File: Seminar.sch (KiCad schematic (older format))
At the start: 0 parts

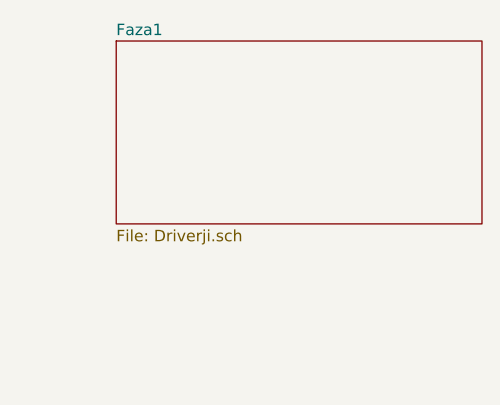
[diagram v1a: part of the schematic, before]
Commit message: Dokončal V-meter sheet in dodal A-meter sheet
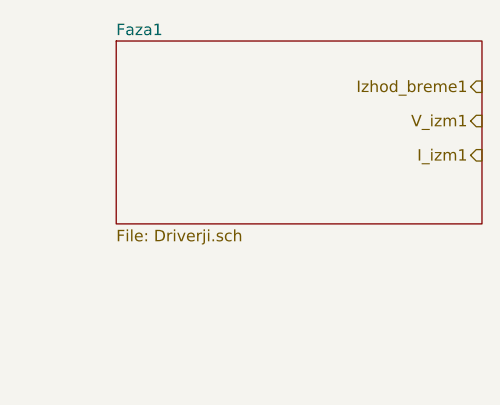
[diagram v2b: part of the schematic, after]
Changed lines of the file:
@@
 $Descr A4 11693 8268
 encoding utf-8
-Sheet 1 4
+Sheet 1 5
 Title ""
 Date ""
@@
 F1 "Driverji.sch" 50
 $EndSheet
+Text HLabel 10500 1450 0    50   Output ~ 0
+Izhod_breme1
+Text HLabel 10500 1600 0    50   Output ~ 0
+V_izm1
+Text HLabel 10500 1750 0    50   Output ~ 0
+I_izm1
 $EndSCHEMATC

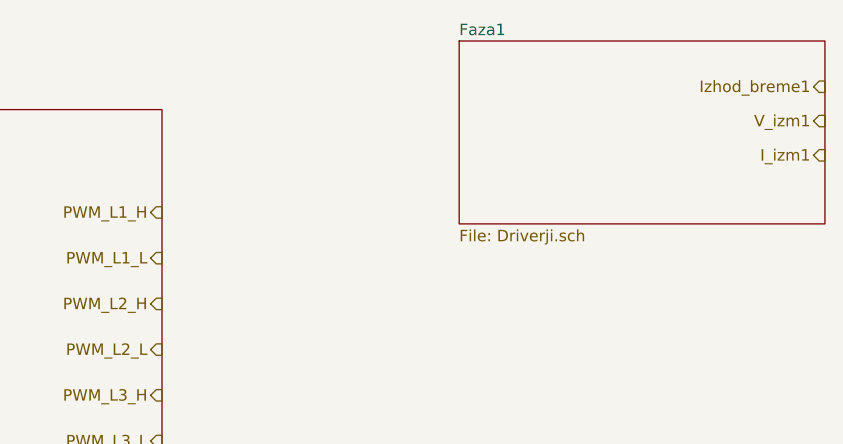
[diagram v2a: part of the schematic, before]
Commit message: Dodano vezje za OC_trip pri merjenju toka
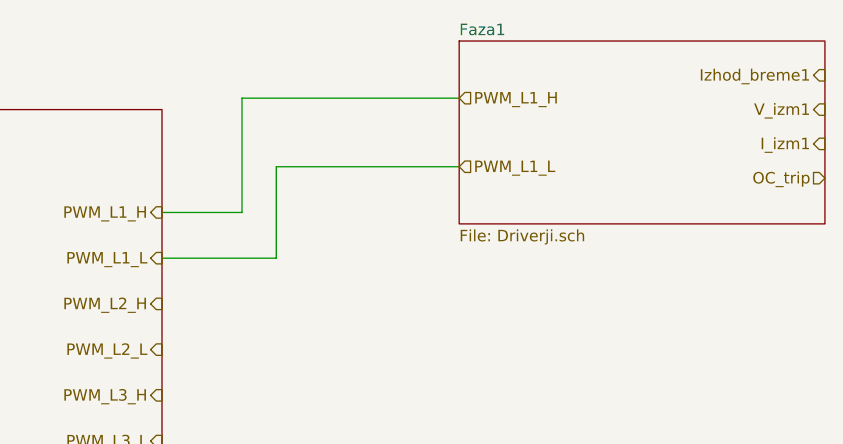
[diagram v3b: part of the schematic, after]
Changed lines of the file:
@@
 F1 "Driverji.sch" 50
 $EndSheet
-Text HLabel 10500 1450 0    50   Output ~ 0
+Text HLabel 10500 1400 0    50   Output ~ 0
 Izhod_breme1
-Text HLabel 10500 1600 0    50   Output ~ 0
+Text HLabel 10500 1550 0    50   Output ~ 0
 V_izm1
-Text HLabel 10500 1750 0    50   Output ~ 0
+Text HLabel 10500 1700 0    50   Output ~ 0
 I_izm1
+Text HLabel 8900 1500 2    50   Input ~ 0
+PWM_L1_H
+Text HLabel 8900 1800 2    50   Input ~ 0
+PWM_L1_L
+Wire Wire Line
+	7600 2000 7950 2000
+Wire Wire Line
+	7950 2000 7950 1500
+Wire Wire Line
+	7950 1500 8900 1500
+Wire Wire Line
+	7600 2200 8100 2200
+Wire Wire Line
+	8100 2200 8100 1800
+Wire Wire Line
+	8100 1800 8900 1800
+Text HLabel 10500 1850 0    50   Input ~ 0
+OC_trip
 $EndSCHEMATC

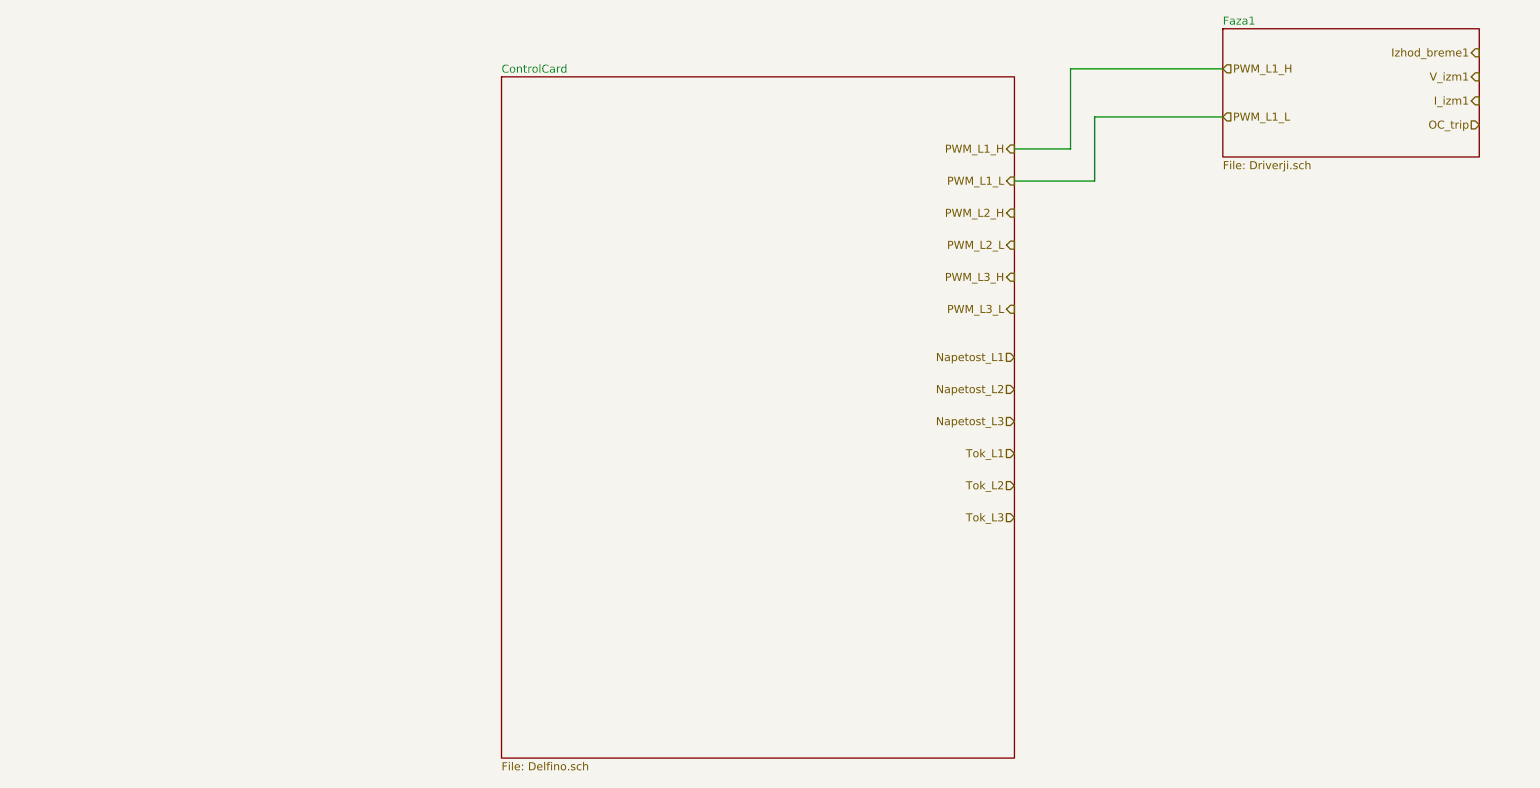
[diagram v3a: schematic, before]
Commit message: Narejene povezave med sheet-i, še vedno nevem kaj z QEP signali
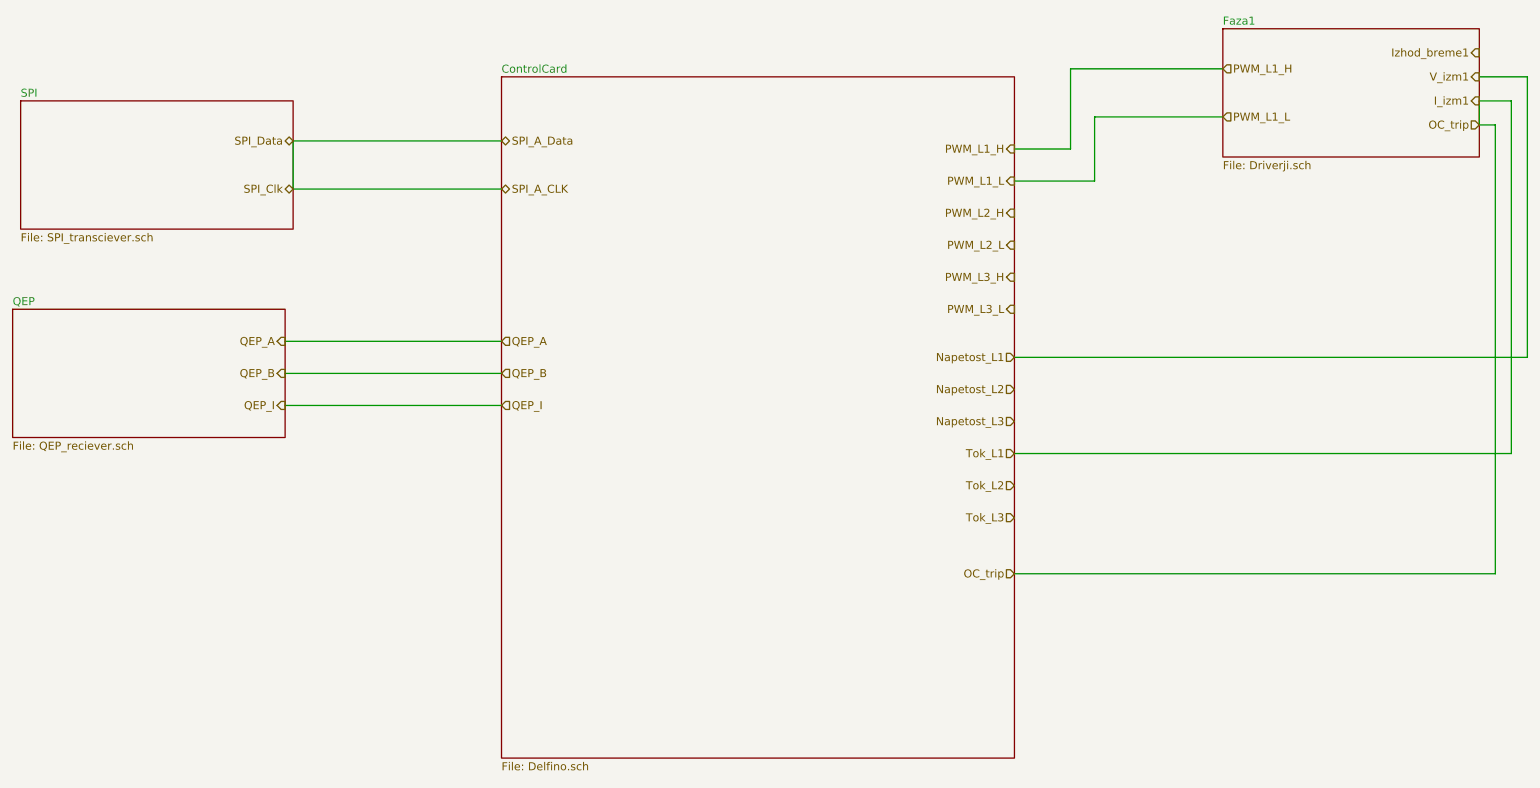
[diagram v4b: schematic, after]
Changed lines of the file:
@@
 $Descr A4 11693 8268
 encoding utf-8
-Sheet 1 5
+Sheet 1 7
 Title ""
 Date ""
@@
 Text HLabel 10500 1850 0    50   Input ~ 0
 OC_trip
+$Sheet
+S 1400 1700 1700 800
+U 5BCFA07B
+F0 "SPI" 50
+F1 "SPI_transciever.sch" 50
+$EndSheet
+$Sheet
+S 1350 3000 1700 800
+U 5BCFA8CE
+F0 "QEP" 50
+F1 "QEP_reciever.sch" 50
+$EndSheet
+Text HLabel 3100 1950 0    50   BiDi ~ 0
+SPI_Data
+Text HLabel 3100 2250 0    50   BiDi ~ 0
+SPI_Clk
+Text HLabel 3050 3200 0    50   Output ~ 0
+QEP_A
+Text HLabel 3050 3400 0    50   Output ~ 0
+QEP_B
+Text HLabel 3050 3600 0    50   Output ~ 0
+QEP_I
+Text HLabel 4400 1950 2    50   BiDi ~ 0
+SPI_A_Data
+Text HLabel 4400 2250 2    50   BiDi ~ 0
+SPI_A_CLK
+Text HLabel 4400 3200 2    50   Input ~ 0
+QEP_A
+Text HLabel 4400 3400 2    50   Input ~ 0
+QEP_B
+Text HLabel 4400 3600 2    50   Input ~ 0
+QEP_I
+Wire Wire Line
+	3050 3200 4400 3200
+Wire Wire Line
+	4400 3400 3050 3400
+Wire Wire Line
+	3050 3600 4400 3600
+Wire Wire Line
+	4400 1950 3100 1950
+Wire Wire Line
+	3100 1950 3100 2250
+Wire Wire Line
+	4400 2250 3100 2250
+Text HLabel 7600 4650 0    50   Input ~ 0
+OC_trip
+Wire Wire Line
+	7600 4650 10600 4650
+Wire Wire Line
+	10600 4650 10600 1850
+Wire Wire Line
+	10500 1850 10600 1850
+Wire Wire Line
+	10500 1850 10500 1700
+Wire Wire Line
+	10500 1700 10700 1700
+Wire Wire Line
+	7600 3900 10700 3900
+Wire Wire Line
+	10700 1700 10700 3900
+Wire Wire Line
+	7600 3300 10800 3300
+Wire Wire Line
+	10800 1550 10800 3300
+Wire Wire Line
+	10500 1550 10800 1550
 $EndSCHEMATC
